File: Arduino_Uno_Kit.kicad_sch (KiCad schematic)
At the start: 34 parts, among them J1 20TW-995, J2 20TW-994, J3 PH2-06-UA, J4 19TW-746, J5 USB-C Serial-Footprint (16U2), J7 ICS-328-T, Q1 2N7000BU, U1 ATMEGA328P-PU, U2 LE33CZ, U3 L7805ABP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

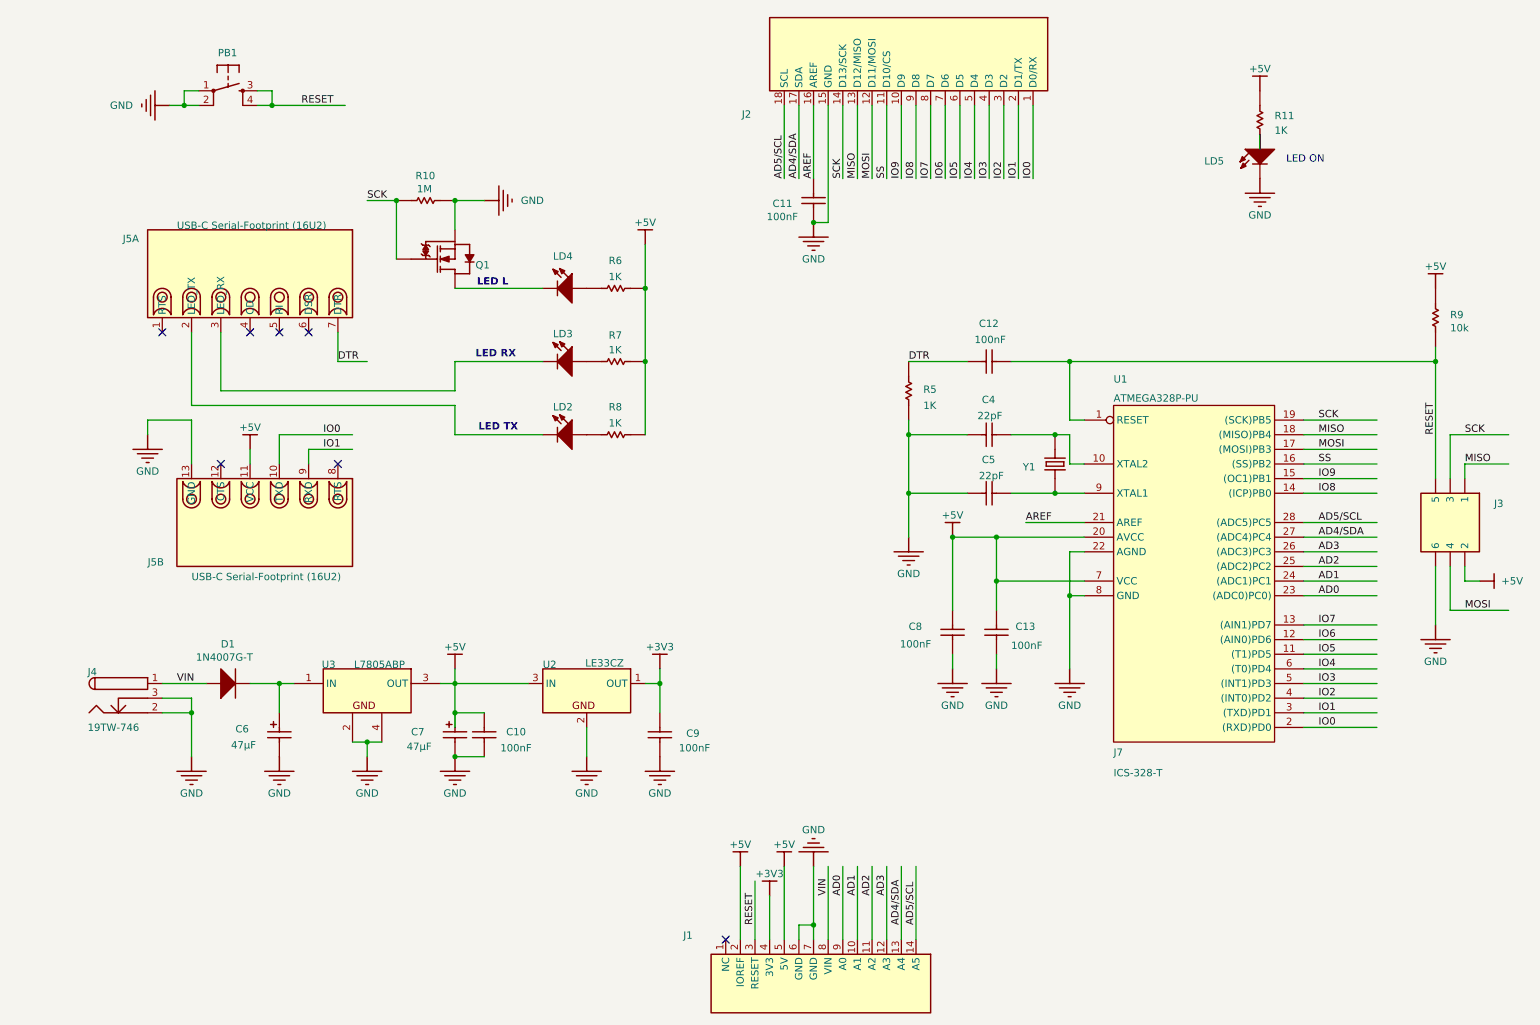
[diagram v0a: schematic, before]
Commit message: seperated into sheets and added usb c serial interface
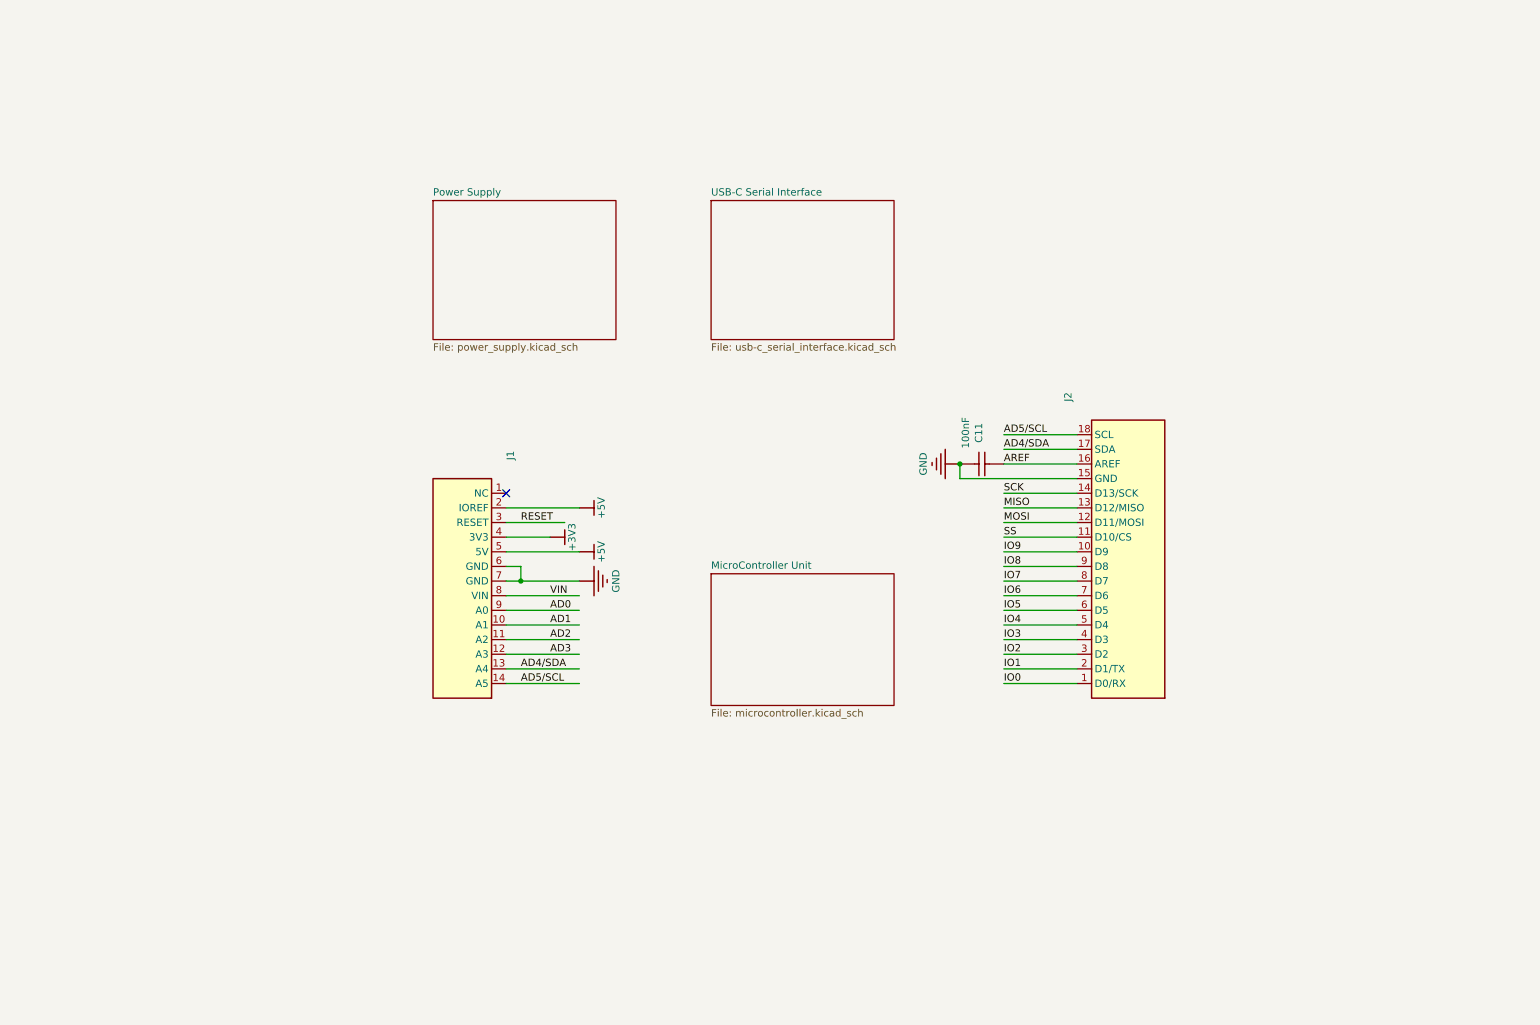
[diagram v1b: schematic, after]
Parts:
- removed C10, C13, C8, C9: B32529C0104J289, B32529C0104J289, symbol Arduino_Uno_Kit-altium-import:3_CAP
- removed C12: B32529C0104J289, B32529C0104J289, symbol Arduino_Uno_Kit-altium-import:2_CAP
- removed C4, C5: TS170R1H220JSANB0R, TS170R1H220JSANB0R, symbol Arduino_Uno_Kit-altium-import:2_CAP
- removed C6, C7: EKF476M1EE05TU, EKF476M1EE05TU, symbol Arduino_Uno_Kit-altium-import:1_CAP-POL
- removed D1: 1N4007G-T, 1N4007G-T-Footprint-1, symbol Arduino_Uno_Kit-altium-import:0_1N4007G-T
- removed J3: PH2-06-UA, 2X03, symbol Arduino_Uno_Kit-altium-import:3_PH2-06-UA
- removed J4: 19TW-746, POWERSUPPLY_DC-21MM, symbol Arduino_Uno_Kit-altium-import:0_19TW-746
- removed J5: USB-C Serial-Footprint (16U2), USB-C Serial-Footprint (16U2), symbol Arduino_Uno_Kit-altium-import:3_USB-C Serial CARRIER
- removed J7: ICS-328-T, ICS-328-T-Footprint-1, symbol Arduino_Uno_Kit-altium-import:0_CMP-003-0010-A.2
- removed LD2, LD3, LD4: L-7104YD, L314YD-Footprint-1, symbol Arduino_Uno_Kit-altium-import:3_LED
- removed LD5: L-7104GD, L314YD-Footprint-1, symbol Arduino_Uno_Kit-altium-import:0_LED
- removed PB1: TS21043-160B-5227260, SW6X6, symbol Arduino_Uno_Kit-altium-import:3_PB-TE
- removed Q1: 2N7000BU, SOT23, symbol Arduino_Uno_Kit-altium-import:2_mirrored_NMOS-2
- removed R10: 3-1623930-5, A5217, symbol Arduino_Uno_Kit-altium-import:0_RES
- removed R11, R5: 2-1623930-9, A5215, symbol Arduino_Uno_Kit-altium-import:3_RES
- removed R6, R7, R8: 2-1623930-9, A5215, symbol Arduino_Uno_Kit-altium-import:2_RES
- removed R9: 0-1623930-3, A5213, symbol Arduino_Uno_Kit-altium-import:1_RES
- removed U1: ATMEGA328P-PU, DIL28-3, symbol Arduino_Uno_Kit-altium-import:0_ATMEGA328P-PU-A.6
- removed U2: LE33CZ, LE33CZ-TR/AP, symbol Arduino_Uno_Kit-altium-import:0_LE33CZ-TR/AP
- removed U3: L7805ABP, TO220, symbol Arduino_Uno_Kit-altium-import:0_L7805CT
- removed Y1: ECS-160-20-4X-DU, ECS-160-20-4X-DU-Footprint-1, symbol Arduino_Uno_Kit-altium-import:1_Crystal
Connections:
- no-connect marks 7 -> 1
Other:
- added sheet MicroController Unit (microcontroller.kicad_sch)
- added sheet Power Supply (power_supply.kicad_sch)
- added sheet USB-C Serial Interface (usb-c_serial_interface.kicad_sch)
- note removed: "LED L"
- note removed: "LED ON"
- note removed: "LED RX"
- note removed: "LED TX"
- moved on the sheet: C11, J1, J2

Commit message: started cleanup, need to do sheet labels
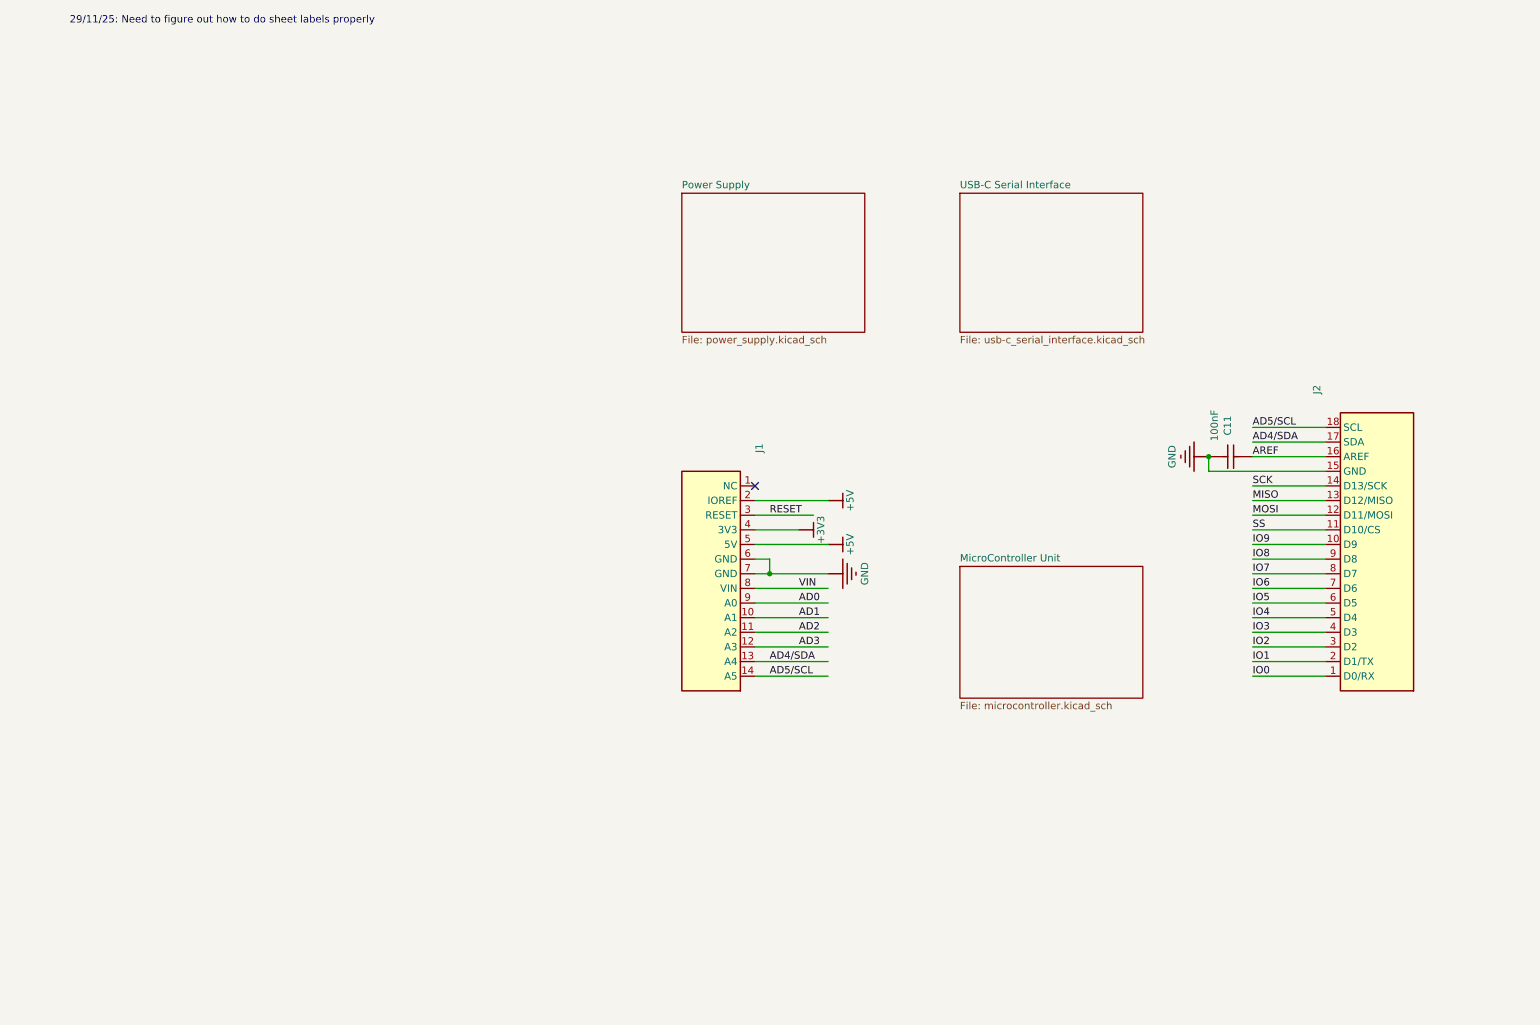
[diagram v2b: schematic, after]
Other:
- note added: "29/11/25: Need to figure out how to do sheet labels properly"
- moved on the sheet: C11, J1, J2
